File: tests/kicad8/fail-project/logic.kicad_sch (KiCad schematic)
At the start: 5 parts, among them U1 74LS04, U2 74AHC1G126, U4 74AHC1G126

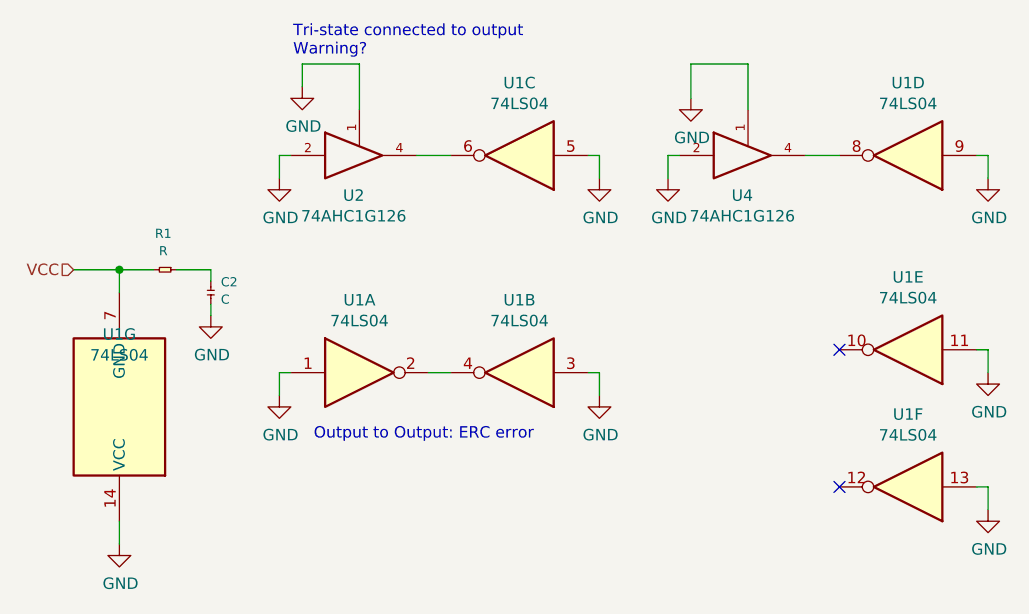
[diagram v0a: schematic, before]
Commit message: [PCBNew][DRC] Implemented CLI version
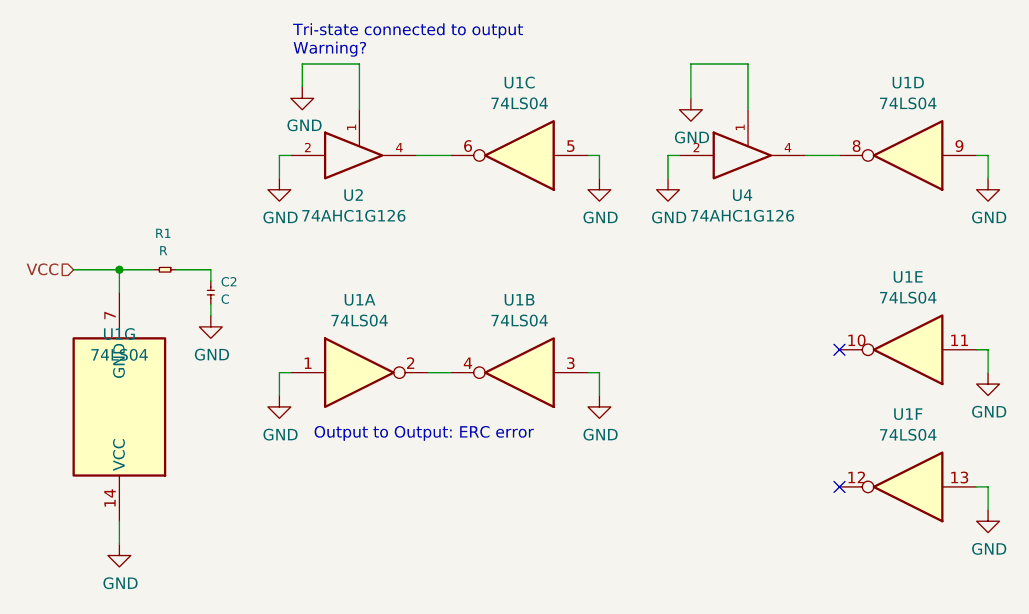
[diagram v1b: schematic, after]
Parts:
- U1: footprint (none) -> Package_SO:SOIC-14_3.9x8.7mm_P1.27mm
- U2, U4: footprint (none) -> Package_TO_SOT_SMD:SOT-23-5
